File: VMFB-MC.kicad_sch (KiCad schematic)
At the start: 52 parts, among them J1 DISPENSE, J12 Conn_01x10_Pin, J2 EMPTY, J3 DISPENSE, J4 DEPOSIT, J5 DISPENSE, J6 EMPTY, J7 MOTOR, J8 PIR, J9 Conn_01x04_Pin, Q1 Q_Photo_NPN, Q10 Q_Photo_NPN, Q2 Q_Photo_NPN, Q3 Q_Photo_NPN, Q4 Q_Photo_NPN, Q5 Q_Photo_NPN, Q6 Q_Photo_NPN, Q7 TIP120, Q8 TIP120, Q9 BC337, U1 LM393

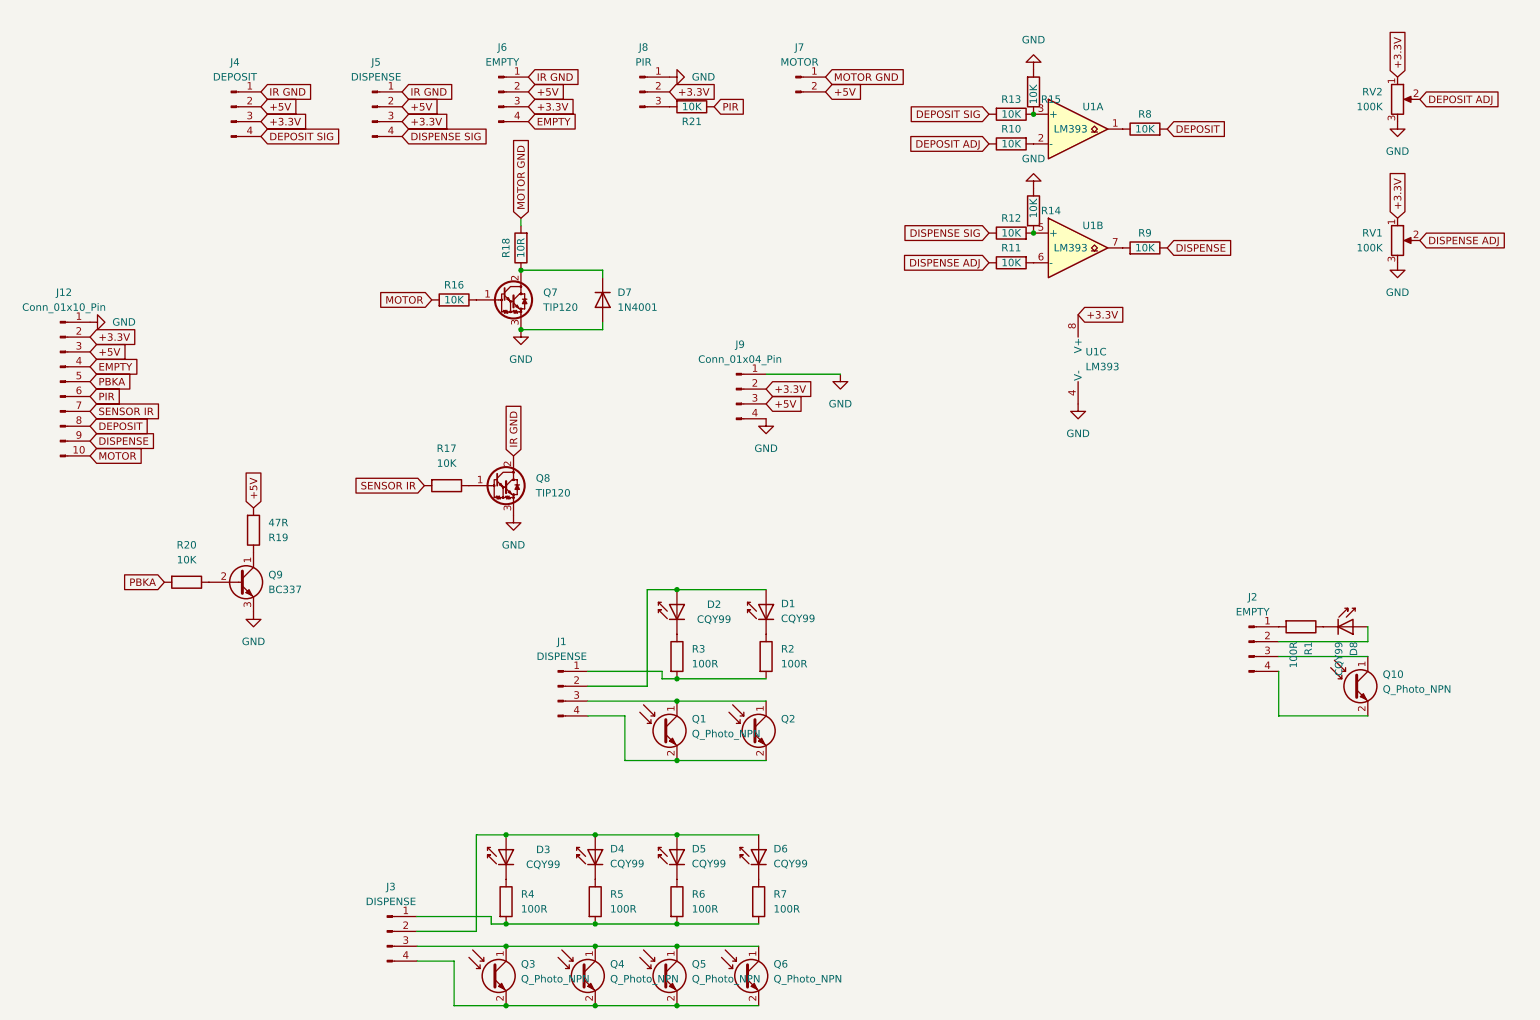
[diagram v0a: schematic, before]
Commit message: New layour and routing
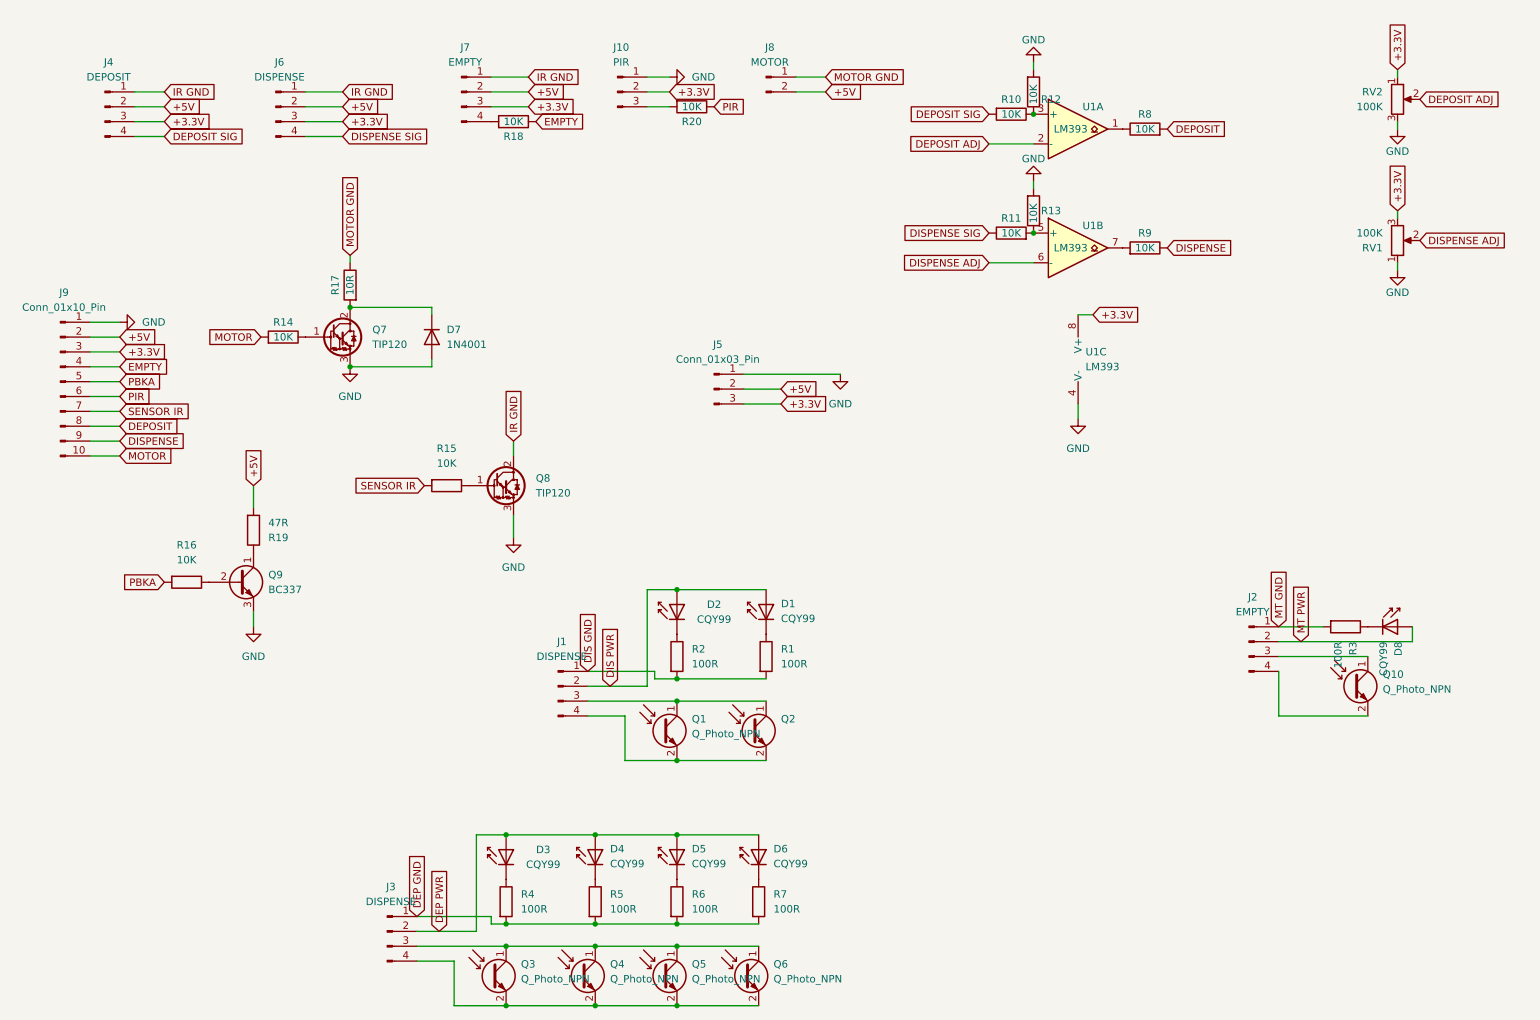
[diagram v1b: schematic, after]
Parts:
- removed J9: Conn_01x04_Pin, Connector_PinHeader_2.54mm:PinHeader_1x04_P2.54mm_Vertical, symbol Connector:Conn_01x04_Pin
- removed R10, R11: 10K, Resistor_THT:R_Axial_DIN0207_L6.3mm_D2.5mm_P2.54mm_Vertical, symbol Device:R
- added J5: Conn_01x03_Pin, Connector_PinHeader_2.54mm:PinHeader_1x03_P2.54mm_Vertical, symbol Connector:Conn_01x03_Pin
- added R18: 10K, Resistor_THT:R_Axial_DIN0207_L6.3mm_D2.5mm_P2.54mm_Vertical, symbol Device:R
- renumbered J8 to J10, J5 to J6, J6 to J7, J7 to J8, J12 to J9, R2 to R1, R13 to R10, R12 to R11, R15 to R12, R14 to R13, R16 to R14, R17 to R15, R20 to R16, R18 to R17, R3 to R2, R21 to R20, R1 to R3
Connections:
- net +3.3V: now also J9.3 (Pin_3), RV1.3, J5.3 (Pin_3); no longer J9.2 (Pin_2), RV1.1
- net +5V: now also J9.2 (Pin_2), J5.2 (Pin_2); no longer J9.3 (Pin_3)
- net DEPOSIT ADJ: now also U1.2 (-)
- net DISPENSE ADJ: now also U1.6 (-)
- net EMPTY: now also R18.1; no longer J7.4 (Pin_4)
- net GND: now also R13.2, RV1.1, J5.1 (Pin_1); no longer R13.1, RV1.3
- net MOTOR GND: now also R17.1; no longer R17.2
- net DIS GND: now reaches J1.1 (Pin_1), R1.2, R2.2
- net MT GND: now reaches J2.1 (Pin_1), R3.2
- net DEP GND: now reaches J3.1 (Pin_1), R4.2, R5.2, R6.2, R7.2
- net at D7.1 (K), Q7.2 (C): now also R17.2; no longer R17.1
- net DEP PWR: now reaches D3.2 (A), D4.2 (A), D5.2 (A), D6.2 (A), J3.2 (Pin_2)
- net MT PWR: now reaches D8.2 (A), J2.2 (Pin_2)
- net DIS PWR: now reaches D1.2 (A), D2.2 (A), J1.2 (Pin_2)
- net at R11.2, U1.5 (+): now also R13.1; no longer R13.2
- new net: J7.4 (Pin_4), R18.2
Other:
- title: (none) -> Vending Machine for Birds
- moved on the sheet: D7, D8, J10, J4, J6, J7, J8, Q7, R14, R17, R3

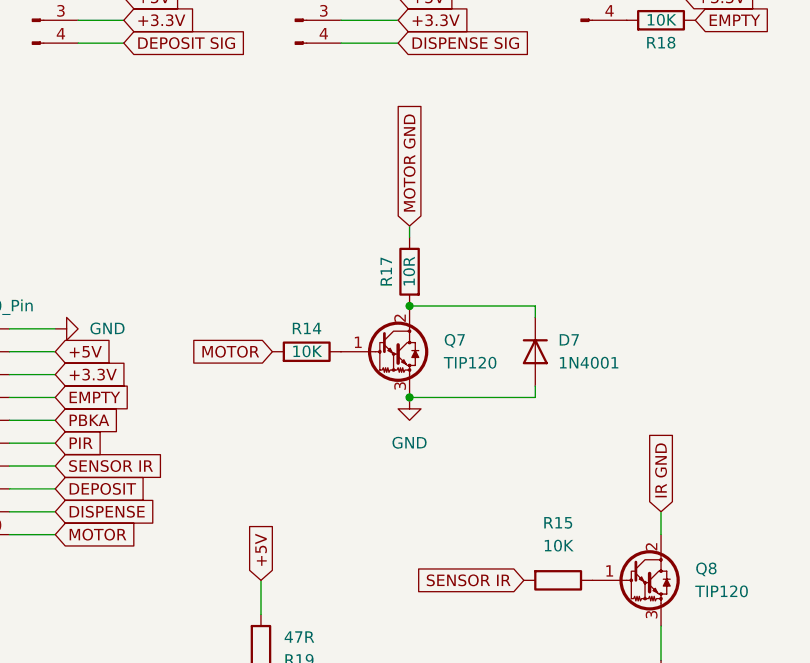
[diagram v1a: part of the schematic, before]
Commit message: updating netclasses, adding routing
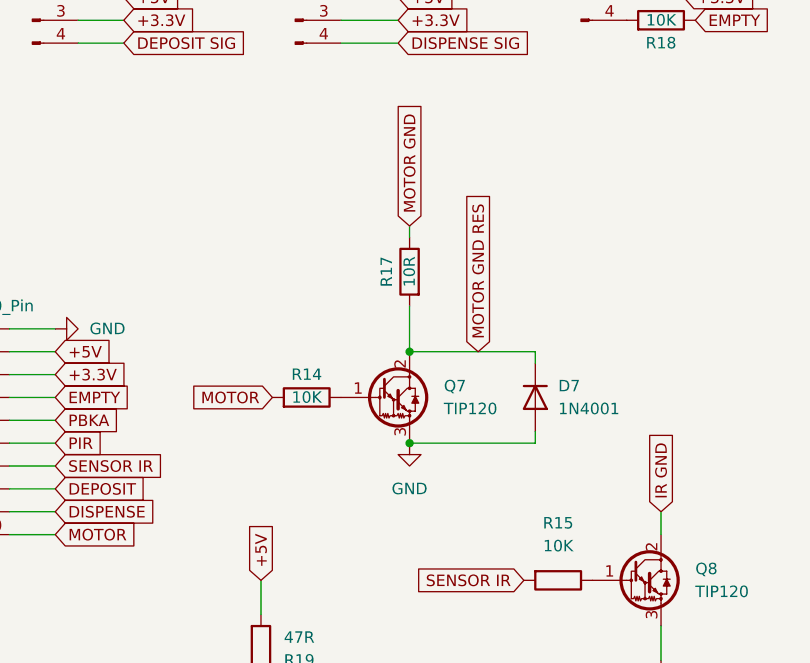
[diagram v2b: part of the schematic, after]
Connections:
- net MOTOR GND RES: now reaches D7.1 (K), Q7.2 (C), R17.2
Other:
- moved on the sheet: D7, Q7, R14
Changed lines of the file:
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@@
   (junction (at 128.27 148.59) (diameter 0) (color 0 0 0 0)
   )
-  (junction (at 72.39 81.28) (diameter 0) (color 0 0 0 0)
+  (junction (at 72.39 76.2) (diameter 0) (color 0 0 0 0)
+  )
+  (junction (at 72.39 86.36) (diameter 0) (color 0 0 0 0)
   )
   (junction (at 189.23 58.42) (diameter 0) (color 0 0 0 0)
@@
   (junction (at 114.3 180.34) (diameter 0) (color 0 0 0 0)
   )
-  (junction (at 72.39 71.12) (diameter 0) (color 0 0 0 0)
-  )
   (junction (at 128.27 134.62) (diameter 0) (color 0 0 0 0)
   )
@@
     (stroke (width 0) (type default))
   )
-  (wire (pts (xy 72.39 81.28) (xy 86.36 81.28))
+  (wire (pts (xy 72.39 86.36) (xy 86.36 86.36))
     (stroke (width 0) (type default))
   )
@@
     (stroke (width 0) (type default))
   )
-  (wire (pts (xy 86.36 71.12) (xy 72.39 71.12))
+  (wire (pts (xy 86.36 76.2) (xy 72.39 76.2))
     (stroke (width 0) (type default))
   )
@@
     (stroke (width 0) (type default))
   )
-  (wire (pts (xy 86.36 72.39) (xy 86.36 71.12))
+  (wire (pts (xy 86.36 77.47) (xy 86.36 76.2))
     (stroke (width 0) (type default))
   )
@@
     (stroke (width 0) (type default))
   )
+  (wire (pts (xy 72.39 76.2) (xy 72.39 71.12))
+    (stroke (width 0) (type default))
+  )
   (wire (pts (xy 128.27 119.38) (xy 143.51 119.38))
     (stroke (width 0) (type default))
@@
     (stroke (width 0) (type default))
   )
-  (wire (pts (xy 86.36 81.28) (xy 86.36 80.01))
+  (wire (pts (xy 86.36 86.36) (xy 86.36 85.09))
     (stroke (width 0) (type default))
   )
@@
     )
   )
+  (global_label "MOTOR GND RES" (shape input) (at 80.01 76.2 90) (fields_autoplaced)
+    (effects (font (size 1.27 1.27)) (justify left))
+    (property "Intersheetrefs" "${INTERSHEET_REFS}" (at 80.01 57.4306 90)
+      (effects (font (size 1.27 1.27)) (justify left) hide)
+    )
+  )
   (global_label "DISPENSE ADJ" (shape input) (at 255.27 59.69 0) (fields_autoplaced)
     (effects (font (size 1.27 1.27)) (justify left))
@@
     )
   )
-  (global_label "MOTOR" (shape input) (at 57.15 76.2 180) (fields_autoplaced)
+  (global_label "MOTOR" (shape input) (at 57.15 81.28 180) (fields_autoplaced)
     (effects (font (size 1.27 1.27)) (justify right))
-    (property "Intersheetrefs" "${INTERSHEET_REFS}" (at 47.8148 76.2 0)
+    (property "Intersheetrefs" "${INTERSHEET_REFS}" (at 47.8148 81.28 0)
       (effects (font (size 1.27 1.27)) (justify right) hide)
     )
@@
     )
   )
-  (symbol (lib_id "Transistor_BJT:TIP120") (at 69.85 76.2 0) (unit 1)
-    (in_bom yes) (on_board yes) (dnp no) (fields_autoplaced)
-    (property "Reference" "Q7" (at 76.2 74.93 0)
-      (effects (font (size 1.27 1.27)) (justify left))
-    )
-    (property "Value" "TIP120" (at 76.2 77.47 0)
-      (effects (font (size 1.27 1.27)) (justify left))
-    )
-    (property "Footprint" "Package_TO_SOT_THT:TO-220-3_Vertical" (at 74.93 78.105 0)
+  (symbol (lib_id "Transistor_BJT:TIP120") (at 69.85 81.28 0) (unit 1)
+    (in_bom yes) (on_board yes) (dnp no) (fields_autoplaced)
+    (property "Reference" "Q7" (at 76.2 80.01 0)
+      (effects (font (size 1.27 1.27)) (justify left))
+    )
+    (property "Value" "TIP120" (at 76.2 82.55 0)
+      (effects (font (size 1.27 1.27)) (justify left))
+    )
+    (property "Footprint" "Package_TO_SOT_THT:TO-220-3_Vertical" (at 74.93 83.185 0)
       (effects (font (size 1.27 1.27) italic) (justify left) hide)
     )
-    (property "Datasheet" "https://www.onsemi.com/pub/Collateral/TIP120-D.PDF" (at 69.85 76.2 0)
+    (property "Datasheet" "https://www.onsemi.com/pub/Collateral/TIP120-D.PDF" (at 69.85 81.28 0)
       (effects (font (size 1.27 1.27)) (justify left) hide)
     )
@@
     )
   )
-  (symbol (lib_id "Diode:1N4001") (at 86.36 76.2 270) (unit 1)
-    (in_bom yes) (on_board yes) (dnp no) (fields_autoplaced)
-    (property "Reference" "D7" (at 88.9 74.93 90)
-      (effects (font (size 1.27 1.27)) (justify left))
-    )
-    (property "Value" "1N4001" (at 88.9 77.47 90)
-      (effects (font (size 1.27 1.27)) (justify left))
-    )
-    (property "Footprint" "Diode_THT:D_DO-41_SOD81_P2.54mm_Vertical_KathodeUp" (at 86.36 76.2 0)
-      (effects (font (size 1.27 1.27)) hide)
-    )
-    (property "Datasheet" "http://www.vishay.com/docs/88503/1n4001.pdf" (at 86.36 76.2 0)
-      (effects (font (size 1.27 1.27)) hide)
-    )
-    (property "Sim.Device" "D" (at 86.36 76.2 0)
-      (effects (font (size 1.27 1.27)) hide)
-    )
-    (property "Sim.Pins" "1=K 2=A" (at 86.36 76.2 0)
+  (symbol (lib_id "Diode:1N4001") (at 86.36 81.28 270) (unit 1)
+    (in_bom yes) (on_board yes) (dnp no) (fields_autoplaced)
+    (property "Reference" "D7" (at 88.9 80.01 90)
+      (effects (font (size 1.27 1.27)) (justify left))
+    )
+    (property "Value" "1N4001" (at 88.9 82.55 90)
+      (effects (font (size 1.27 1.27)) (justify left))
+    )
+    (property "Footprint" "Diode_THT:D_DO-41_SOD81_P2.54mm_Vertical_KathodeUp" (at 86.36 81.28 0)
+      (effects (font (size 1.27 1.27)) hide)
+    )
+    (property "Datasheet" "http://www.vishay.com/docs/88503/1n4001.pdf" (at 86.36 81.28 0)
+      (effects (font (size 1.27 1.27)) hide)
+    )
+    (property "Sim.Device" "D" (at 86.36 81.28 0)
+      (effects (font (size 1.27 1.27)) hide)
+    )
+    (property "Sim.Pins" "1=K 2=A" (at 86.36 81.28 0)
       (effects (font (size 1.27 1.27)) hide)
     )
@@
     )
   )
-  (symbol (lib_id "Device:R") (at 60.96 76.2 270) (mirror x) (unit 1)
+  (symbol (lib_id "Device:R") (at 60.96 81.28 270) (mirror x) (unit 1)
     (in_bom yes) (on_board yes) (dnp no)
-    (property "Reference" "R14" (at 60.96 73.66 90)
-      (effects (font (size 1.27 1.27)))
-    )
-    (property "Value" "10K" (at 60.96 76.2 90)
-      (effects (font (size 1.27 1.27)))
-    )
-    (property "Footprint" "Resistor_THT:R_Axial_DIN0207_L6.3mm_D2.5mm_P2.54mm_Vertical" (at 60.96 77.978 90)
-      (effects (font (size 1.27 1.27)) hide)
-    )
-    (property "Datasheet" "~" (at 60.96 76.2 0)
+    (property "Reference" "R14" (at 60.96 78.74 90)
+      (effects (font (size 1.27 1.27)))
+    )
+    (property "Value" "10K" (at 60.96 81.28 90)
+      (effects (font (size 1.27 1.27)))
+    )
+    (property "Footprint" "Resistor_THT:R_Axial_DIN0207_L6.3mm_D2.5mm_P2.54mm_Vertical" (at 60.96 83.058 90)
+      (effects (font (size 1.27 1.27)) hide)
+    )
+    (property "Datasheet" "~" (at 60.96 81.28 0)
       (effects (font (size 1.27 1.27)) hide)
     )
@@
     )
   )
-  (symbol (lib_id "power:GND") (at 72.39 81.28 0) (unit 1)
-    (in_bom yes) (on_board yes) (dnp no) (fields_autoplaced)
-    (property "Reference" "#PWR03" (at 72.39 87.63 0)
-      (effects (font (size 1.27 1.27)) hide)
-    )
-    (property "Value" "GND" (at 72.39 86.36 0)
-      (effects (font (size 1.27 1.27)))
-    )
-    (property "Footprint" "" (at 72.39 81.28 0)
-      (effects (font (size 1.27 1.27)) hide)
-    )
-    (property "Datasheet" "" (at 72.39 81.28 0)
-      (effects (font (size 1.27 1.27)) hide)
-    )
+  (symbol (lib_id "power:GND") (at 72.39 86.36 0) (unit 1)
+    (in_bom yes) (on_board yes) (dnp no) (fields_autoplaced)
+    (property "Reference" "#PWR03" (at 72.39 92.71 0)
+      (effects (font (size 1.27 1.27)) hide)
+    )
+    (property "Value" "GND" (at 72.39 91.44 0)
+      (effects (font (size 1.27 1.27)))
+    )
+    (property "Footprint" "" (at 72.39 86.36 0)
+      (effects (font (size 1.27 1.27)) hide)
+    )
+    (property "Datasheet" "" (at 72.39 86.36 0)
+      (effects (font (size 1.27 1.27)) hide)
+    )
